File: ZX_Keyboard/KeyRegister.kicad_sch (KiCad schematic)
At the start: 73 parts

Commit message: improve schematic
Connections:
- net SCLK renamed SCK
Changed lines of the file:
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@@
     (effects (font (size 1.27 1.27)) (justify left bottom))
   )
-  (label "KA14" (at 38.0808 105.41 180)
+  (label "KA14" (at 38.1 105.41 180)
     (effects (font (size 1.27 1.27)) (justify right bottom))
   )
@@
     (effects (font (size 1.27 1.27)) (justify left bottom))
   )
-  (label "KA15" (at 37.8482 107.95 180)
+  (label "KA15" (at 38.1 107.95 180)
     (effects (font (size 1.27 1.27)) (justify right bottom))
   )
@@
     (effects (font (size 1.27 1.27)) (justify right))
   )
-  (hierarchical_label "SCLK" (shape input) (at 25.4 41.91 180)
+  (hierarchical_label "SCK" (shape input) (at 25.4 41.91 180)
     (effects (font (size 1.27 1.27)) (justify right))
   )
@@
   (symbol (lib_id "power:VCC") (at 20.32 82.55 0) (unit 1)
     (in_bom yes) (on_board yes) (fields_autoplaced)
-    (property "Reference" "#PWR037" (id 0) (at 20.32 86.36 0)
-      (effects (font (size 1.27 1.27)) hide)
-    )
+    (property "Reference" "#PWR038" (id 0) (at 20.32 86.36 0)
+      (effects (font (size 1.27 1.27)) hide)
+    )

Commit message: update and fix schematic
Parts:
- added CKR1, CKR2, CKR3, CKR4, CKR5, CKR6, CKR7, CKR8: 100nF, Capacitor_SMD:C_0805_2012Metric_Pad1.18x1.45mm_HandSolder, symbol Device:C
- added CKR10, CKR9: 4.7uFx6.3V, Capacitor_Tantalum_SMD:CP_EIA-3528-21_Kemet-B_Pad1.50x2.35mm_HandSolder, symbol Device:C_Polarized
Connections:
- net GND: now also CKR1.2, CKR10.2, CKR2.2, CKR3.2, CKR4.2, CKR5.2, CKR6.2, CKR7.2, CKR8.2, CKR9.2
- net LOAD: now also UKR2.12 (STORE), UKR4.12 (STORE), UKR6.12 (STORE), UKR8.12 (STORE)
- net KA10 renamed KeyA10
- net KA11 renamed KeyA11
- net KA12 renamed KeyA12
- net KA13 renamed KeyA13
- net KA14 renamed KeyA14
- net KA15 renamed KeyA15
- net KA8 renamed KeyA8
- net KA9 renamed KeyA9
- net KD0 renamed KeyD0
- net KD1 renamed KeyD1
- net KD2 renamed KeyD2
- net KD3 renamed KeyD3
- net KD4 renamed KeyD4
- net KD5 renamed KeyD5
- net KD6 renamed KeyD6
- net KD7 renamed KeyD7
- new net +3.3V: CKR1.1, CKR10.1, CKR2.1, CKR3.1, CKR4.1, CKR5.1, CKR6.1, CKR7.1, CKR8.1, CKR9.1
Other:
- moved on the sheet: DKR1, DKR10, DKR11, DKR12, DKR13, DKR14, DKR15, DKR16, DKR17, DKR18, DKR19, DKR2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

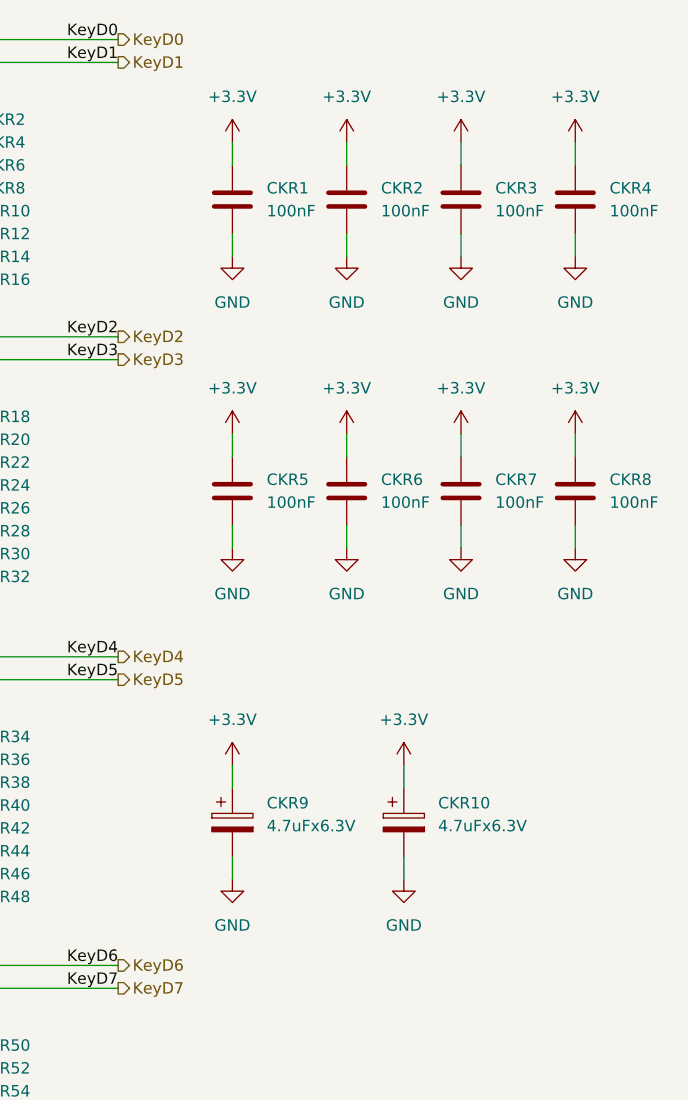
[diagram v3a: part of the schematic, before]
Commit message: update schema trace pcb
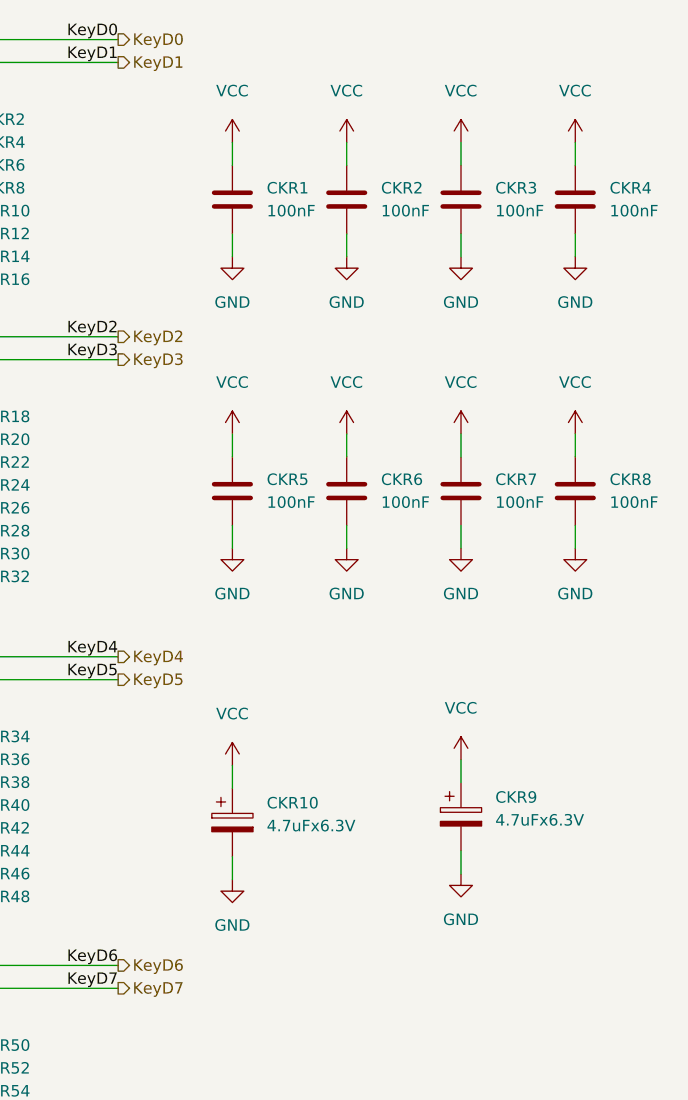
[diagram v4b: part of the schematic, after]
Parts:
- renumbered CKR9 to CKR10, CKR10 to CKR9
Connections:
- net +3.3V is gone; now on net VCC: CKR1.1, CKR10.1, CKR2.1, CKR3.1, CKR4.1, CKR5.1, CKR6.1, CKR7.1, CKR8.1, CKR9.1
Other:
- moved on the sheet: CKR9

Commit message: update schematic and pcb
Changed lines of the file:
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@@
-    (stroke (width 0) (type default) (color 0 0 0 0))
-  )
-  (wire (pts (xy 113.03 137.16) (xy 111.76 137.16))
     (stroke (width 0) (type default) (color 0 0 0 0))
   )

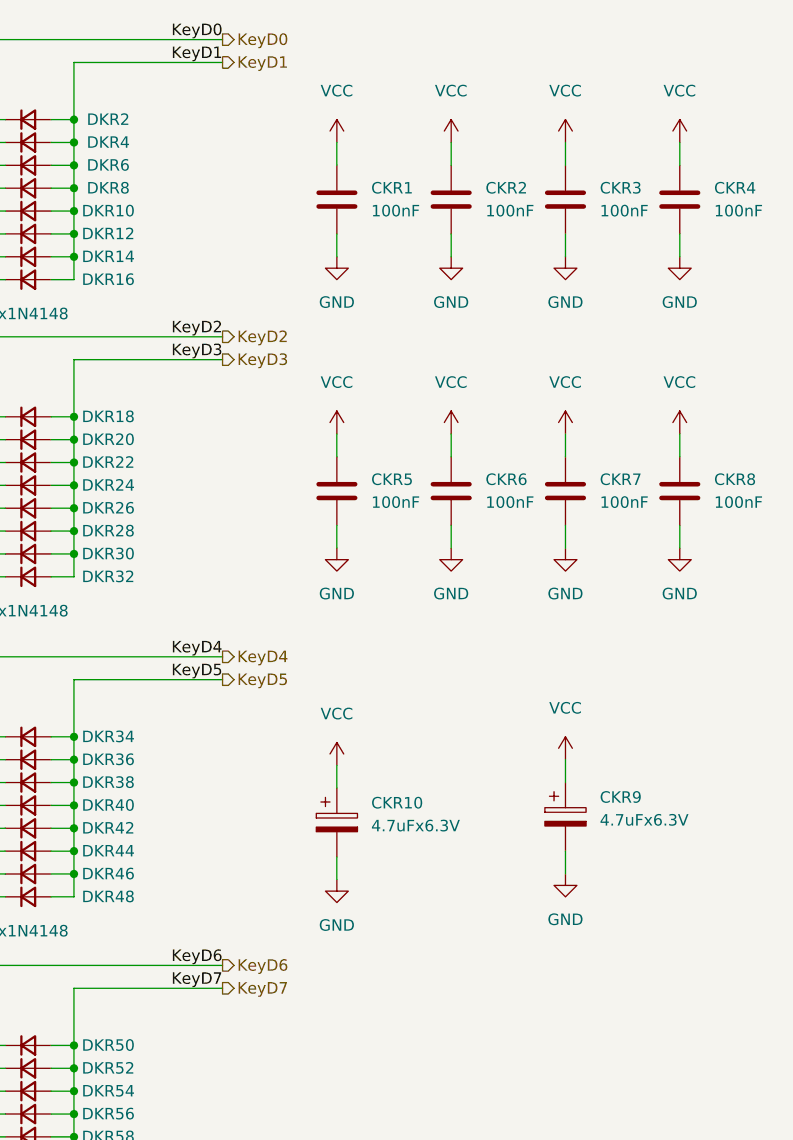
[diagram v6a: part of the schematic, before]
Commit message: fix keyboard connectors
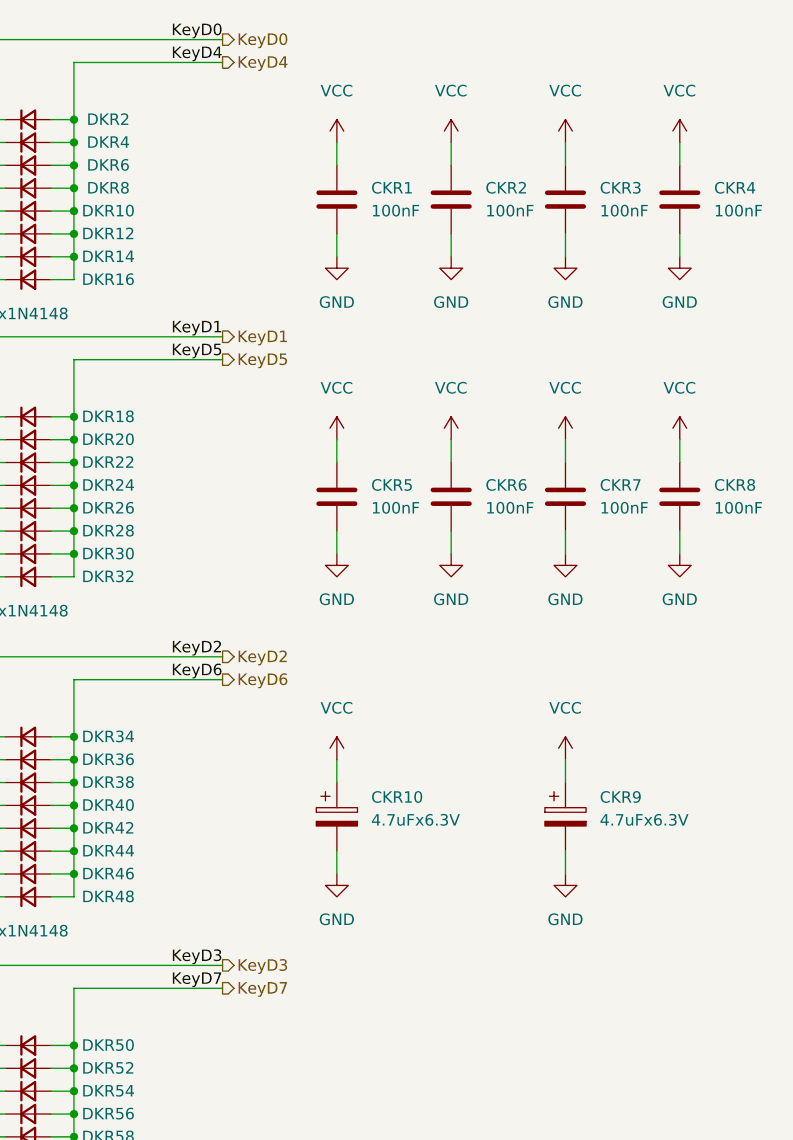
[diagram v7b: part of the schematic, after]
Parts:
- CKR10, CKR9: footprint Capacitor_Tantalum_SMD:CP_EIA-3528-21_Kemet-B_Pad1.50x2.35mm_HandSolder -> Capacitor_Tantalum_SMD:CP_EIA-3216-18_Kemet-A_Pad1.58x1.35mm_HandSolder
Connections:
- net KeyD1: now also DKR17.2 (A), DKR19.2 (A), DKR21.2 (A), DKR23.2 (A), DKR25.2 (A), DKR27.2 (A), DKR29.2 (A), DKR31.2 (A); no longer DKR10.2 (A), DKR12.2 (A), DKR14.2 (A), DKR16.2 (A), DKR2.2 (A), DKR4.2 (A), DKR6.2 (A), DKR8.2 (A)
- net KeyD2: now also DKR33.2 (A), DKR35.2 (A), DKR37.2 (A), DKR39.2 (A), DKR41.2 (A), DKR43.2 (A), DKR45.2 (A), DKR47.2 (A); no longer DKR17.2 (A), DKR19.2 (A), DKR21.2 (A), DKR23.2 (A), DKR25.2 (A), DKR27.2 (A), DKR29.2 (A), DKR31.2 (A)
- net KeyD3: now also DKR49.2 (A), DKR51.2 (A), DKR53.2 (A), DKR55.2 (A), DKR57.2 (A), DKR59.2 (A), DKR61.2 (A), DKR63.2 (A); no longer DKR18.2 (A), DKR20.2 (A), DKR22.2 (A), DKR24.2 (A), DKR26.2 (A), DKR28.2 (A), DKR30.2 (A), DKR32.2 (A)
- net KeyD4: now also DKR10.2 (A), DKR12.2 (A), DKR14.2 (A), DKR16.2 (A), DKR2.2 (A), DKR4.2 (A), DKR6.2 (A), DKR8.2 (A); no longer DKR33.2 (A), DKR35.2 (A), DKR37.2 (A), DKR39.2 (A), DKR41.2 (A), DKR43.2 (A), DKR45.2 (A), DKR47.2 (A)
- net KeyD5: now also DKR18.2 (A), DKR20.2 (A), DKR22.2 (A), DKR24.2 (A), DKR26.2 (A), DKR28.2 (A), DKR30.2 (A), DKR32.2 (A); no longer DKR34.2 (A), DKR36.2 (A), DKR38.2 (A), DKR40.2 (A), DKR42.2 (A), DKR44.2 (A), DKR46.2 (A), DKR48.2 (A)
- net KeyD6: now also DKR34.2 (A), DKR36.2 (A), DKR38.2 (A), DKR40.2 (A), DKR42.2 (A), DKR44.2 (A), DKR46.2 (A), DKR48.2 (A); no longer DKR49.2 (A), DKR51.2 (A), DKR53.2 (A), DKR55.2 (A), DKR57.2 (A), DKR59.2 (A), DKR61.2 (A), DKR63.2 (A)
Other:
- moved on the sheet: CKR10, CKR5, CKR6, CKR7, CKR8

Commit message: update keyboard pcb
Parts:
- renumbered CKR9 to CKR10, CKR10 to CKR9
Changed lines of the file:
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@@
   (symbol (lib_id "power:VCC") (at 234.95 31.75 0) (unit 1)
     (in_bom yes) (on_board yes) (fields_autoplaced)
-    (property "Reference" "#PWR038" (id 0) (at 234.95 35.56 0)
+    (property "Reference" "#PWR040" (id 0) (at 234.95 35.56 0)
       (effects (font (size 1.27 1.27)) hide)
     )
@@
   (symbol (lib_id "power:VCC") (at 273.05 64.77 0) (unit 1)
     (in_bom yes) (on_board yes) (fields_autoplaced)
-    (property "Reference" "#PWR049" (id 0) (at 273.05 68.58 0)
+    (property "Reference" "#PWR051" (id 0) (at 273.05 68.58 0)
       (effects (font (size 1.27 1.27)) hide)
     )
@@
   (symbol (lib_id "power:VCC") (at 247.65 64.77 0) (unit 1)
     (in_bom yes) (on_board yes) (fields_autoplaced)
-    (property "Reference" "#PWR047" (id 0) (at 247.65 68.58 0)
+    (property "Reference" "#PWR049" (id 0) (at 247.65 68.58 0)
       (effects (font (size 1.27 1.27)) hide)
     )
@@
   (symbol (lib_id "power:GND") (at 247.65 44.45 0) (unit 1)
     (in_bom yes) (on_board yes) (fields_autoplaced)
-    (property "Reference" "#PWR043" (id 0) (at 247.65 50.8 0)
+    (property "Reference" "#PWR045" (id 0) (at 247.65 50.8 0)
       (effects (font (size 1.27 1.27)) hide)
     )
@@
   (symbol (lib_id "power:VCC") (at 16.51 82.55 0) (unit 1)
     (in_bom yes) (on_board yes) (fields_autoplaced)
-    (property "Reference" "#PWR054" (id 0) (at 16.51 86.36 0)
+    (property "Reference" "#PWR056" (id 0) (at 16.51 86.36 0)
       (effects (font (size 1.27 1.27)) hide)
     )
@@
   (symbol (lib_id "power:GND") (at 260.35 113.03 0) (unit 1)
     (in_bom yes) (on_board yes) (fields_autoplaced)
-    (property "Reference" "#PWR057" (id 0) (at 260.35 119.38 0)
+    (property "Reference" "#PWR060" (id 0) (at 260.35 119.38 0)
       (effects (font (size 1.27 1.27)) hide)
     )
@@
   (symbol (lib_id "power:VCC") (at 234.95 64.77 0) (unit 1)
     (in_bom yes) (on_board yes) (fields_autoplaced)
-    (property "Reference" "#PWR046" (id 0) (at 234.95 68.58 0)
+    (property "Reference" "#PWR048" (id 0) (at 234.95 68.58 0)
       (effects (font (size 1.27 1.27)) hide)
     )
@@
   (symbol (lib_id "power:GND") (at 260.35 77.47 0) (unit 1)
     (in_bom yes) (on_board yes) (fields_autoplaced)
-    (property "Reference" "#PWR052" (id 0) (at 260.35 83.82 0)
+    (property "Reference" "#PWR054" (id 0) (at 260.35 83.82 0)
       (effects (font (size 1.27 1.27)) hide)
     )
@@
   (symbol (lib_id "power:GND") (at 234.95 77.47 0) (unit 1)
     (in_bom yes) (on_board yes) (fields_autoplaced)
-    (property "Reference" "#PWR050" (id 0) (at 234.95 83.82 0)
+    (property "Reference" "#PWR052" (id 0) (at 234.95 83.82 0)
       (effects (font (size 1.27 1.27)) hide)
     )
@@
   (symbol (lib_id "power:GND") (at 234.95 44.45 0) (unit 1)
     (in_bom yes) (on_board yes) (fields_autoplaced)
-    (property "Reference" "#PWR042" (id 0) (at 234.95 50.8 0)
+    (property "Reference" "#PWR044" (id 0) (at 234.95 50.8 0)
       (effects (font (size 1.27 1.27)) hide)
     )
@@
   (symbol (lib_id "power:GND") (at 273.05 77.47 0) (unit 1)
     (in_bom yes) (on_board yes) (fields_autoplaced)
-    (property "Reference" "#PWR053" (id 0) (at 273.05 83.82 0)
+    (property "Reference" "#PWR055" (id 0) (at 273.05 83.82 0)
       (effects (font (size 1.27 1.27)) hide)
     )
@@
   (symbol (lib_id "power:VCC") (at 260.35 64.77 0) (unit 1)
     (in_bom yes) (on_board yes) (fields_autoplaced)
-    (property "Reference" "#PWR048" (id 0) (at 260.35 68.58 0)
+    (property "Reference" "#PWR050" (id 0) (at 260.35 68.58 0)
       (effects (font (size 1.27 1.27)) hide)
     )
@@
   (symbol (lib_id "Device:C_Polarized") (at 234.95 106.68 0) (unit 1)
     (in_bom yes) (on_board yes) (fields_autoplaced)
-    (property "Reference" "CKR10" (id 0) (at 238.76 104.5209 0)
+    (property "Reference" "CKR9" (id 0) (at 238.76 104.5209 0)
       (effects (font (size 1.27 1.27)) (justify left))
     )
@@
   (symbol (lib_id "power:VCC") (at 260.35 31.75 0) (unit 1)
     (in_bom yes) (on_board yes) (fields_autoplaced)
-    (property "Reference" "#PWR040" (id 0) (at 260.35 35.56 0)
+    (property "Reference" "#PWR042" (id 0) (at 260.35 35.56 0)
       (effects (font (size 1.27 1.27)) hide)
     )
@@
   (symbol (lib_id "Device:C_Polarized") (at 260.35 106.68 0) (unit 1)
     (in_bom yes) (on_board yes) (fields_autoplaced)
-    (property "Reference" "CKR9" (id 0) (at 264.16 104.5209 0)
+    (property "Reference" "CKR10" (id 0) (at 264.16 104.5209 0)
       (effects (font (size 1.27 1.27)) (justify left))
     )
@@
   (symbol (lib_id "power:GND") (at 273.05 44.45 0) (unit 1)
     (in_bom yes) (on_board yes) (fields_autoplaced)
-    (property "Reference" "#PWR045" (id 0) (at 273.05 50.8 0)
+    (property "Reference" "#PWR047" (id 0) (at 273.05 50.8 0)
       (effects (font (size 1.27 1.27)) hide)
     )
@@
   (symbol (lib_id "power:VCC") (at 234.95 100.33 0) (unit 1)
     (in_bom yes) (on_board yes) (fields_autoplaced)
-    (property "Reference" "#PWR056" (id 0) (at 234.95 104.14 0)
+    (property "Reference" "#PWR057" (id 0) (at 234.95 104.14 0)
       (effects (font (size 1.27 1.27)) hide)
     )
@@
   (symbol (lib_id "power:VCC") (at 273.05 31.75 0) (unit 1)
     (in_bom yes) (on_board yes) (fields_autoplaced)
-    (property "Reference" "#PWR041" (id 0) (at 273.05 35.56 0)
+    (property "Reference" "#PWR043" (id 0) (at 273.05 35.56 0)
       (effects (font (size 1.27 1.27)) hide)
     )
@@
   (symbol (lib_id "power:GND") (at 260.35 44.45 0) (unit 1)
     (in_bom yes) (on_board yes) (fields_autoplaced)
-    (property "Reference" "#PWR044" (id 0) (at 260.35 50.8 0)
+    (property "Reference" "#PWR046" (id 0) (at 260.35 50.8 0)
       (effects (font (size 1.27 1.27)) hide)
     )
@@
   (symbol (lib_id "power:VCC") (at 260.35 100.33 0) (unit 1)
     (in_bom yes) (on_board yes) (fields_autoplaced)
-    (property "Reference" "#PWR055" (id 0) (at 260.35 104.14 0)
+    (property "Reference" "#PWR058" (id 0) (at 260.35 104.14 0)
       (effects (font (size 1.27 1.27)) hide)
     )
@@
   (symbol (lib_id "power:GND") (at 247.65 77.47 0) (unit 1)
     (in_bom yes) (on_board yes) (fields_autoplaced)
-    (property "Reference" "#PWR051" (id 0) (at 247.65 83.82 0)
+    (property "Reference" "#PWR053" (id 0) (at 247.65 83.82 0)
       (effects (font (size 1.27 1.27)) hide)
     )
@@
   (symbol (lib_id "power:VCC") (at 247.65 31.75 0) (unit 1)
     (in_bom yes) (on_board yes) (fields_autoplaced)
-    (property "Reference" "#PWR039" (id 0) (at 247.65 35.56 0)
+    (property "Reference" "#PWR041" (id 0) (at 247.65 35.56 0)
       (effects (font (size 1.27 1.27)) hide)
     )
@@
   (symbol (lib_id "power:GND") (at 234.95 113.03 0) (unit 1)
     (in_bom yes) (on_board yes) (fields_autoplaced)
-    (property "Reference" "#PWR058" (id 0) (at 234.95 119.38 0)
-      (effects (font (size 1.27 1.27)) hide)
-    )
+    (property "Reference" "#PWR059" (id 0) (at 234.95 119.38 0)
+      (effects (font (size 1.27 1.27)) hide)
+    )
